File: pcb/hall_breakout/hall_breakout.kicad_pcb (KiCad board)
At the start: 2 copper layers, 14 x 12.4 mm, 6 parts, among them J1 to controller J4, U1 A3144

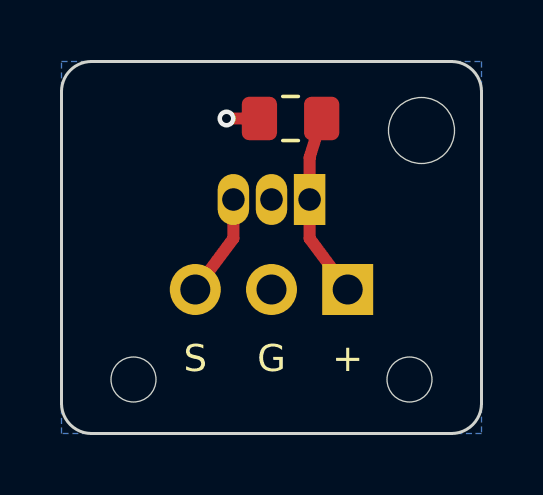
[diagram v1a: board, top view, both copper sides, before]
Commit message: Move the hall board's M2 hole clear of the mirror clamp
An M2 screw through the old hole at (12.0, 2.3) would hit the mirror
clamp inside the head. At (1.8, 5.0) an M2 x 5 clears it by 1.1 mm, as
measured in the CAD. The hole gets its own footprint with a courtyard
the size of the screw head, and the cable pads' courtyard is trimmed to
the usual 0.25 mm, so the two fit side by side. The README gives the
new pilot-hole position on the head and notes what cad/ now has.
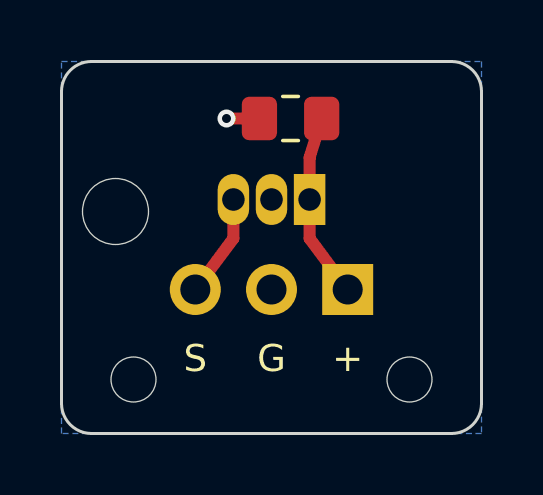
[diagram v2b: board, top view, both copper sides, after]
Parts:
- H1: footprint rig:MountingHole_2.2mm_M2 -> rig:Hole_M2_2.2mm
- moved H1 10.6 mm to (101.8, 105.0)
